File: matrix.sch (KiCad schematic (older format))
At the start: 147 parts

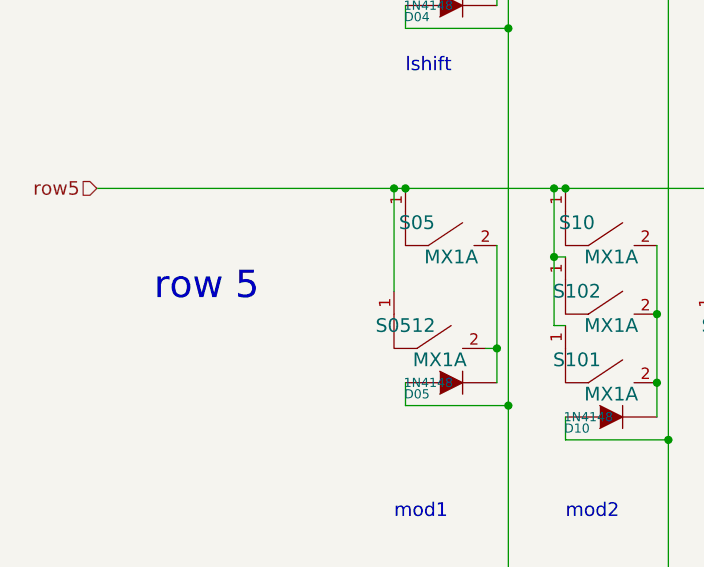
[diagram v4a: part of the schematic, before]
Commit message: Remove SW0512
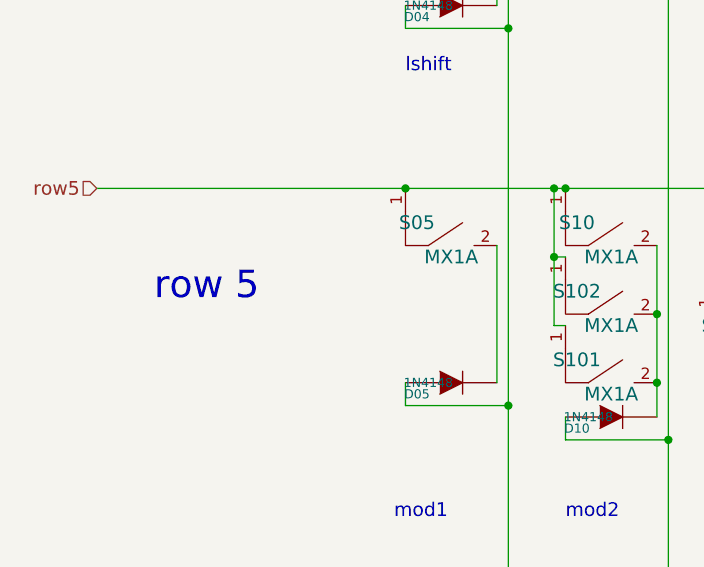
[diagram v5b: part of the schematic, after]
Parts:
- removed S0512: MX1A, mx1a:MX1A_no3d, symbol mx1a-simple:MX1A
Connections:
- wire segments 405 -> 401
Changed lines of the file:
@@
-$EndComp
-$Comp
-L mx1a-simple:MX1A S0512
-U 1 1 5040ECF7
-P 3300 9000
-F 0 "S0512" H 3150 9250 60  0000 C CNN
-F 1 "MX1A" H 3300 9100 60  0000 C CNN
-F 2 "mx1a:MX1A_no3d" H 3300 9000 60  0001 C CNN
-F 3 "" H 3300 9000 60  0001 C CNN
-	1    3300 9000
-	1    0    0    -1
 $EndComp
 $Comp
@@
 Connection ~ 3850 8150
 Connection ~ 3150 8150
-Wire Wire Line
-	1800 8150 3100 8150
 Connection ~ 12250 6650
 Connection ~ 10850 6650
@@
 Connection ~ 6600 8150
 Wire Wire Line
-	3550 8400 3550 8850
-Connection ~ 3100 8150
-Wire Wire Line
-	3550 8850 3500 8850
-Wire Wire Line
 	4950 8850 4900 8850
 Wire Wire Line
@@
 	4550 9100 5000 9100
 Connection ~ 4950 8850
-Connection ~ 3550 8850
 Wire Wire Line
 	4550 9000 4550 9100
@@
 	6600 8150 6650 8150
 Wire Wire Line
-	3100 8150 3150 8150
-Wire Wire Line
 	3100 5150 3150 5150
 Wire Wire Line
@@
 	4950 8850 4950 9000
 Wire Wire Line
-	3550 8850 3550 9000
-Wire Wire Line
 	12650 8850 12650 9000
 Wire Wire Line
@@
 Wire Wire Line
 	12200 7100 12200 7250
-Wire Wire Line
-	3100 8150 3100 8600
 Wire Wire Line
 	6650 8150 10100 8150
@@
 Wire Wire Line
 	1800 6650 3150 6650
+Wire Wire Line
+	1800 8150 3150 8150
+Wire Wire Line
+	3550 8400 3550 9000
 $EndSCHEMATC

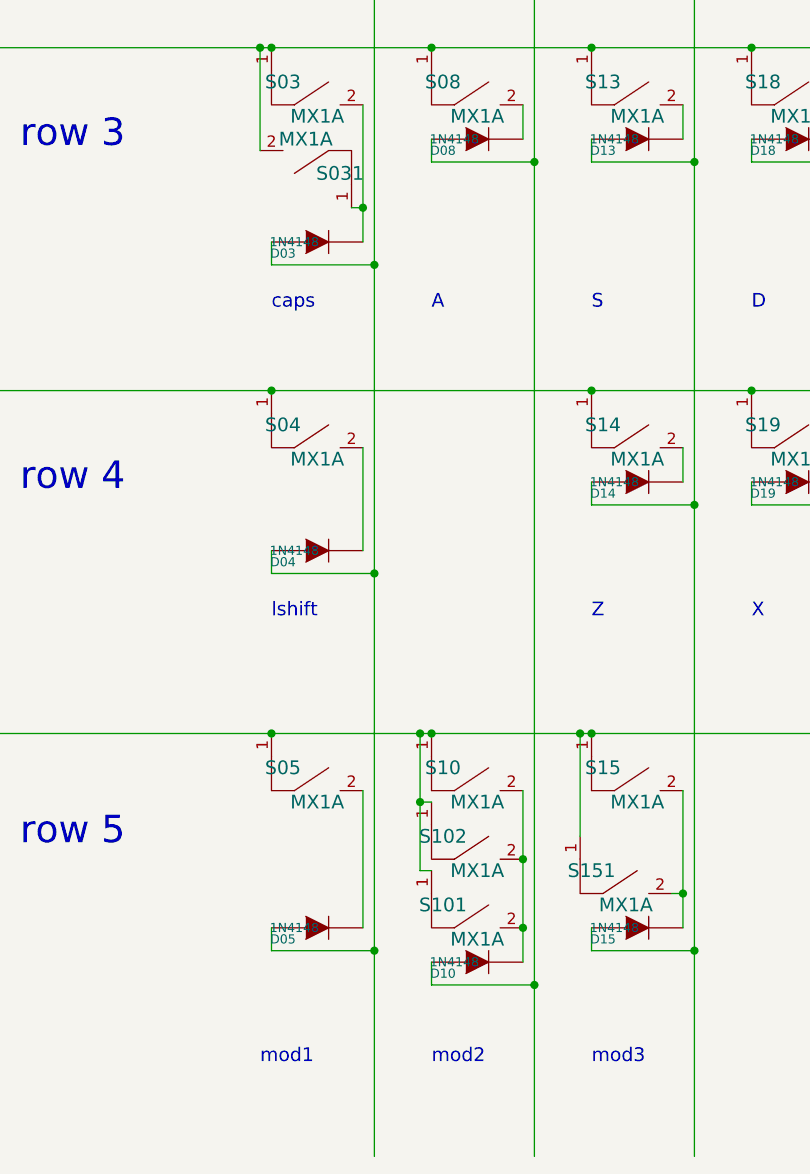
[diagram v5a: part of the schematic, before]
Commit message: Remove unnecessary related SWs to S10
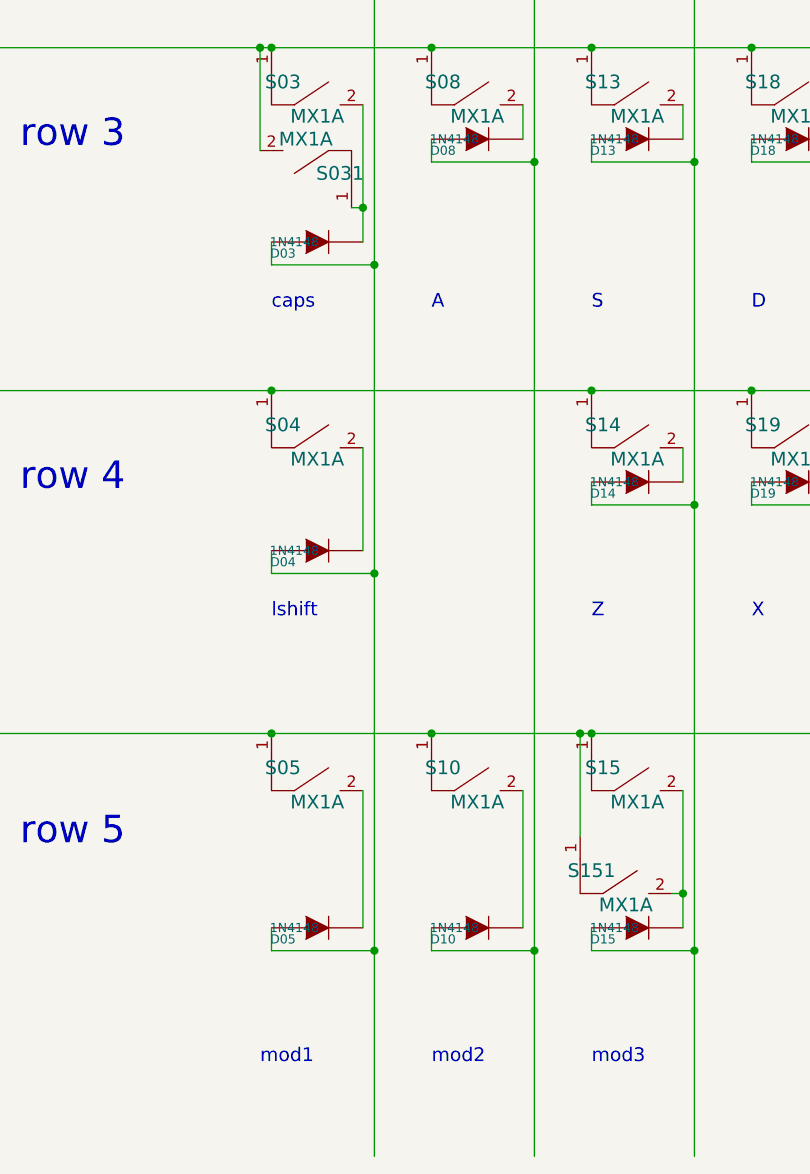
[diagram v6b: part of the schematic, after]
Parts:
- removed S101, S102: MX1A, mx1a:MX1A_no3d, symbol mx1a-simple:MX1A
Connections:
- wire segments 401 -> 394
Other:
- moved on the sheet: D10
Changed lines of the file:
@@
-$EndComp
-$Comp
-L mx1a-simple:MX1A S102
-U 1 1 5040EEA3
-P 4050 8850
-F 0 "S102" H 3900 9100 60  0000 C CNN
-F 1 "MX1A" H 4050 8950 60  0000 C CNN
-F 2 "mx1a:MX1A_no3d" H 4050 8850 60  0001 C CNN
-F 3 "" H 4050 8850 60  0001 C CNN
-	1    4050 8850
-	1    0    0    -1
-$EndComp
-$Comp
-L mx1a-simple:MX1A S101
-U 1 1 5040EEA9
-P 4050 9150
-F 0 "S101" H 3900 9400 60  0000 C CNN
-F 1 "MX1A" H 4050 9250 60  0000 C CNN
-F 2 "mx1a:MX1A_no3d" H 4050 9150 60  0001 C CNN
-F 3 "" H 4050 9150 60  0001 C CNN
-	1    4050 9150
-	1    0    0    -1
 $EndComp
 $Comp
@@
 L device:DIODE D10
 U 1 1 506B5A94
-P 4050 9150
-F 0 "D10" H 3900 9100 40  0000 C CNN
-F 1 "1N4148" H 3950 9150 40  0000 C CNN
-F 2 "0805:0805D" H 4050 9150 60  0001 C CNN
-F 3 "" H 4050 9150 60  0001 C CNN
-F 4 "DC Components" H 3500 5050 60  0001 C CNN "Vendor"
-F 5 "CD4148WS(0805C)" H 3500 5050 60  0001 C CNN "Product"
-F 6 "TME" H 3500 5050 60  0001 C CNN "Supplier"
-F 7 "1N4148-0805" H 3500 5050 60  0001 C CNN "Supplier Symbol"
-	1    4050 9150
+P 4050 9000
+F 0 "D10" H 3900 8950 40  0000 C CNN
+F 1 "1N4148" H 3950 9000 40  0000 C CNN
+F 2 "0805:0805D" H 4050 9000 60  0001 C CNN
+F 3 "" H 4050 9000 60  0001 C CNN
+F 4 "DC Components" H 3500 4900 60  0001 C CNN "Vendor"
+F 5 "CD4148WS(0805C)" H 3500 4900 60  0001 C CNN "Product"
+F 6 "TME" H 3500 4900 60  0001 C CNN "Supplier"
+F 7 "1N4148-0805" H 3500 4900 60  0001 C CNN "Supplier Symbol"
+	1    4050 9000
 	1    0    0    -1
 $EndComp
@@
 Wire Wire Line
 	3600 1400 3600 3450
-Wire Wire Line
-	3800 8750 3850 8750
-Connection ~ 3800 8150
-Wire Wire Line
-	3800 8150 3800 8450
 Connection ~ 4500 8150
 Wire Wire Line
@@
 Connection ~ 11250 8700
 Wire Wire Line
-	4250 8400 4250 8700
-Wire Wire Line
 	1800 5150 3100 5150
 Wire Wire Line
@@
 	3150 9100 3600 9100
 Wire Wire Line
-	3850 9150 3850 9250
-Wire Wire Line
-	3850 9250 4300 9250
+	3850 9000 3850 9100
+Wire Wire Line
+	3850 9100 4300 9100
 Wire Wire Line
 	4550 9100 5000 9100
@@
 Connection ~ 5000 7150
 Connection ~ 3600 9100
-Connection ~ 4300 9250
 Connection ~ 5000 9100
 Connection ~ 5700 3450
@@
 Connection ~ 12650 5700
 Connection ~ 11950 7200
-Connection ~ 4250 9000
 Connection ~ 3550 5850
 Connection ~ 9450 5150
@@
 Wire Wire Line
 	12250 3450 12250 3350
-Wire Wire Line
-	3850 8450 3800 8450
-Connection ~ 3800 8450
-Connection ~ 4250 8700
 Connection ~ 7050 8750
 Wire Wire Line
@@
 Connection ~ 12200 7100
 Wire Wire Line
-	3800 8150 3850 8150
-Wire Wire Line
 	4500 8150 4550 8150
 Wire Wire Line
@@
 	3850 8150 4500 8150
 Wire Wire Line
-	3150 8150 3800 8150
-Wire Wire Line
 	12250 6650 13250 6650
 Wire Wire Line
@@
 	3600 9100 3600 10000
 Wire Wire Line
-	4300 9250 4300 10000
-Wire Wire Line
 	5000 9100 5000 10000
 Wire Wire Line
@@
 	11950 7200 11950 7350
 Wire Wire Line
-	4250 9000 4250 9150
-Wire Wire Line
 	3550 5850 3550 6000
 Wire Wire Line
@@
 Wire Wire Line
 	12650 7500 12650 7650
-Wire Wire Line
-	3800 8450 3800 8750
-Wire Wire Line
-	4250 8700 4250 9000
 Wire Wire Line
 	7050 8750 7050 9200
@@
 	3150 6650 4550 6650
 Wire Wire Line
-	4300 5650 4300 9250
+	4300 5650 4300 9100
 Wire Wire Line
 	3600 7450 3600 9100
@@
 Wire Wire Line
 	3550 8400 3550 9000
+Wire Wire Line
+	4250 8400 4250 9000
+Wire Wire Line
+	3150 8150 3850 8150
+Connection ~ 4300 9100
+Wire Wire Line
+	4300 9100 4300 10000
 $EndSCHEMATC

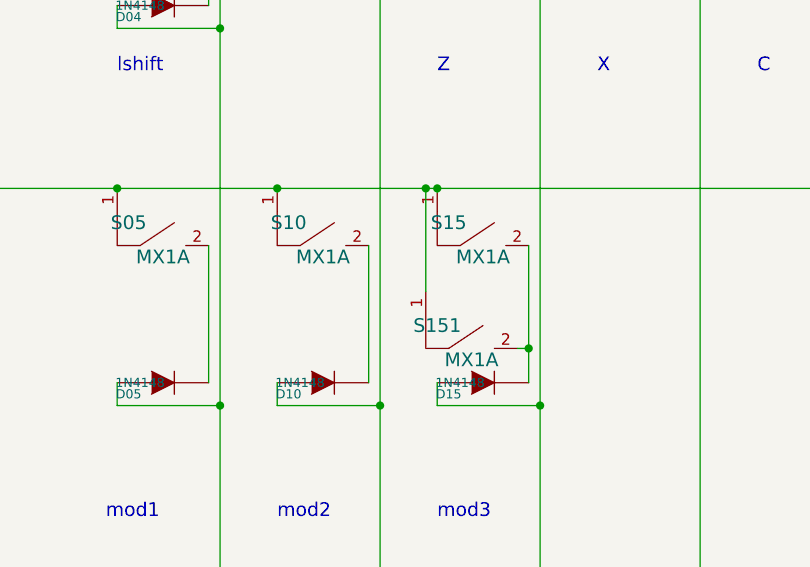
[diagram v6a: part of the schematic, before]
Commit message: Remove unnecessary related SW to SW15
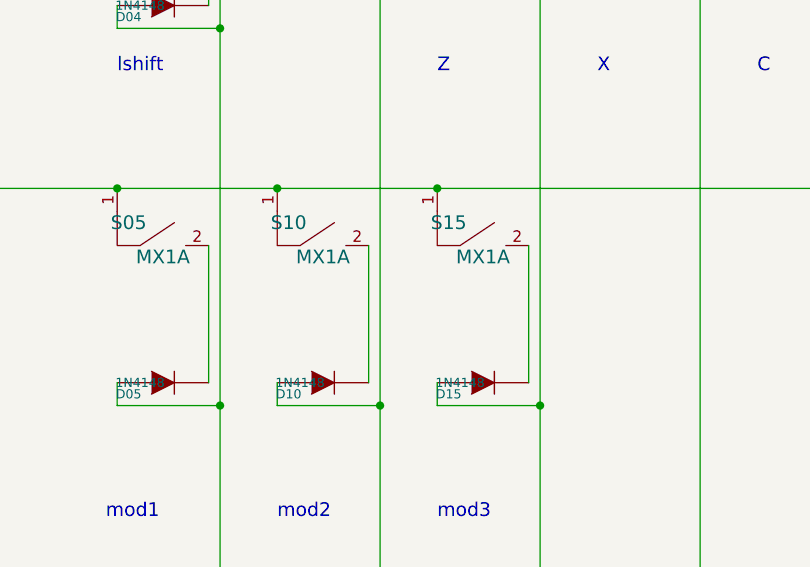
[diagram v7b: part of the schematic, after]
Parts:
- removed S151: MX1A, mx1a:MX1A_no3d, symbol mx1a-simple:MX1A
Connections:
- wire segments 394 -> 390
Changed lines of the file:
@@
-$EndComp
-$Comp
-L mx1a-simple:MX1A S151
-U 1 1 5040F14F
-P 4700 9000
-F 0 "S151" H 4550 9250 60  0000 C CNN
-F 1 "MX1A" H 4700 9100 60  0000 C CNN
-F 2 "mx1a:MX1A_no3d" H 4700 9000 60  0001 C CNN
-F 3 "" H 4700 9000 60  0001 C CNN
-	1    4700 9000
-	1    0    0    -1
 $EndComp
 $Comp
@@
 Wire Wire Line
 	3600 1400 3600 3450
-Connection ~ 4500 8150
-Wire Wire Line
-	4500 8150 4500 8600
 Connection ~ 10100 8150
 Wire Wire Line
@@
 Connection ~ 6600 8150
 Wire Wire Line
-	4950 8850 4900 8850
-Wire Wire Line
 	10550 8850 10500 8850
 Wire Wire Line
@@
 Connection ~ 9450 6650
 Wire Wire Line
-	4950 8400 4950 8850
-Wire Wire Line
 	7800 1400 7800 3450
 Wire Wire Line
@@
 Wire Wire Line
 	4550 9100 5000 9100
-Connection ~ 4950 8850
 Wire Wire Line
 	4550 9000 4550 9100
@@
 Connection ~ 12200 7100
 Wire Wire Line
-	4500 8150 4550 8150
-Wire Wire Line
 	10100 8150 10150 8150
 Wire Wire Line
@@
 	4550 8150 6600 8150
 Wire Wire Line
-	3850 8150 4500 8150
-Wire Wire Line
 	12250 6650 13250 6650
 Wire Wire Line
@@
 Wire Wire Line
 	9450 6650 10150 6650
-Wire Wire Line
-	4950 8850 4950 9000
 Wire Wire Line
 	12650 8850 12650 9000
@@
 Wire Wire Line
 	4300 9100 4300 10000
+Wire Wire Line
+	3850 8150 4550 8150
+Wire Wire Line
+	4950 8400 4950 9000
 $EndSCHEMATC
